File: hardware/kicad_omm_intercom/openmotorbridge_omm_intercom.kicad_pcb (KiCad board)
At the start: 2 copper layers, 60 x 30 mm, 18 parts, among them J1 TYPE-C-31-M-12_IP67, SW1 Power_MFB, SW2 Mesh_Group, SW3 Vol_Plus, SW4 Vol_Minus, U1 ESP32-C6-MINI-1U, U2 BQ24075RGTR, U3 XC6206P332MR, U4 ES8311_Codec

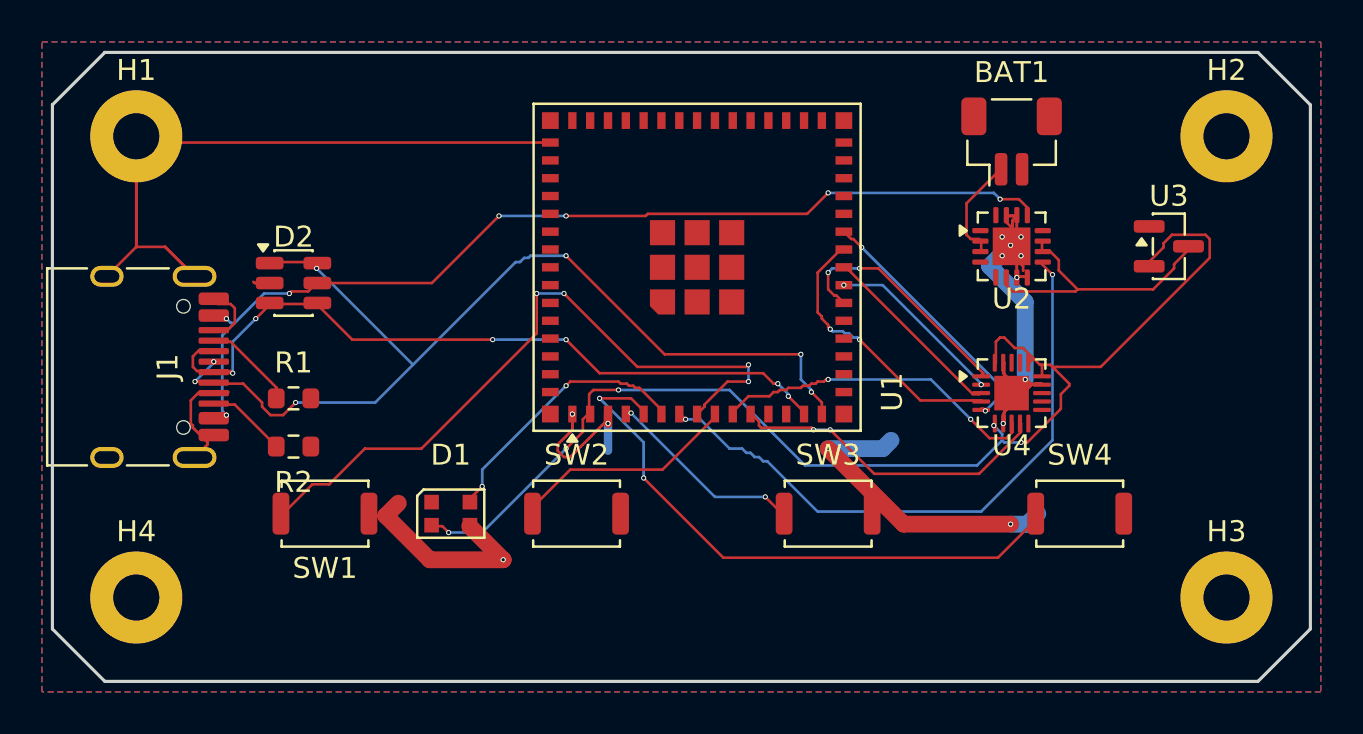
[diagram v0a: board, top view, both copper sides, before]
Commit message: feat(system): architecture refinement v6 across hardware, firmware and docs
- Hardware:
  * PCBA 09 (OMM 2.4 GHz Intercom): Upgrade to Everest Semi ES8388 stereo codec (QFN-28)
    and Multi-Use USB-C connector (J1) combining power, WebUSB flashing and stereo audio.
  * PCBA 08 (Radar 2.0 Sub-MCU): Strict HF hardening (2x U.FL: 6.5 GHz UWB & 5.9 GHz V2X;
    no 2.4 GHz/BLE at rear), right-angle 4-pin flashing header J3.
  * PCBA 03 (Cartridge): 8-pin Kelvin-grounded audio/power header with isolated PGND/AGND.
  * CAD: Standardize DIN 934 hex nut pockets across module enclosures.

- Firmware:
  * UWB Backbone: Add multi-channel substream audio downlink (sub-channels 0/1 music,
    sub-channel 2 voice) and audio uplink packet definitions.
  * Smart Cartridge: Implement zero-latency (<1 ms) voice routing to intercom mic pin,
    A2DP music stream buffering for mesh group sharing, and 100 Hz upstream audio capture.
  * Central Box: Central DSP mixer ducking (-18 dB), voice activity detection (VAD), and
    multi-channel UWB dispatching.
  * OMM Module: Implement ES8388 stereo codec driver and I2S master duplex stream.
  * Radar Sub-MCU: Confirm 2.4 GHz RF disable and autonomous emergency strobe trigger (<1 ms).

- Documentation & WebApp:
  * Align DE & EN chapters (01, 02, 03, 04b, 07, 08, 14, 15, 16) with v6 specifications.
  * Update WebApp PWA System Builder with ES8388 stereo codec and OMM 446 PMR/DMR module.
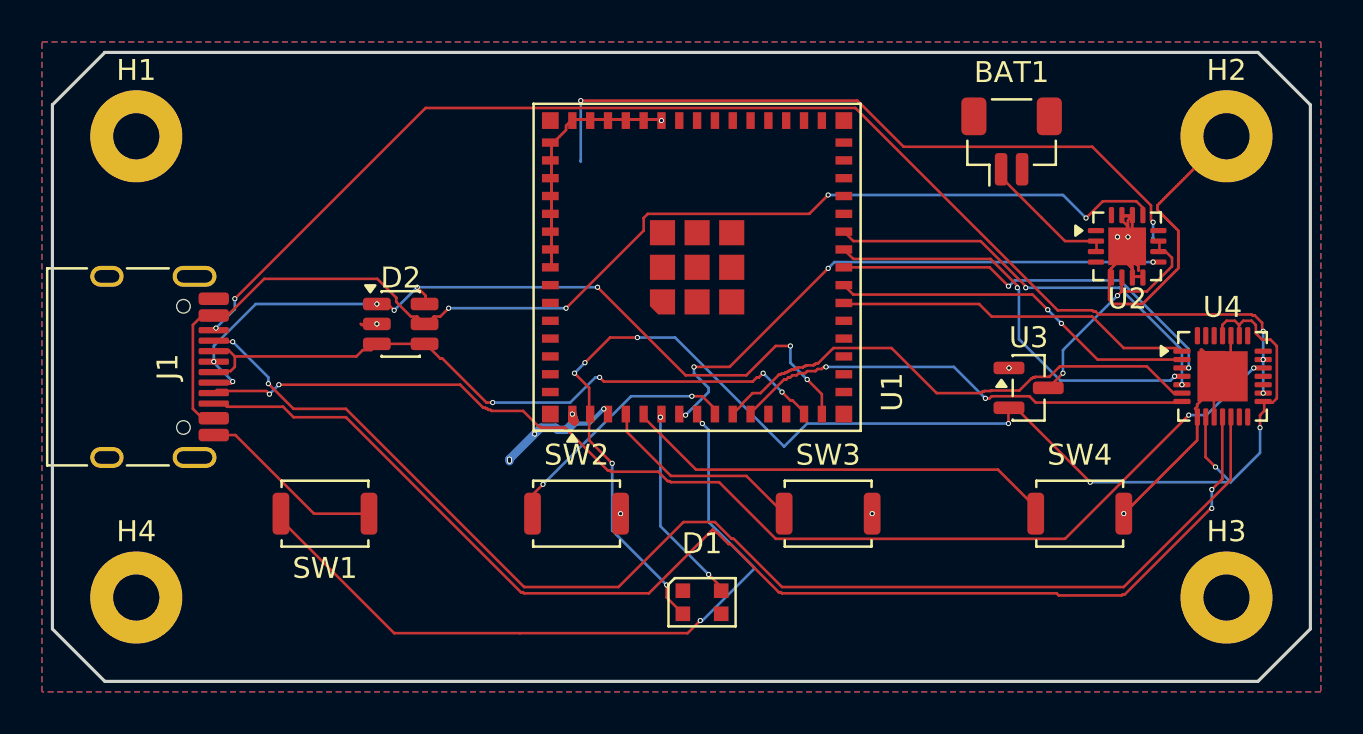
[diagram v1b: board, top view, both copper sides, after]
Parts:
- removed R1: 5.1k_CC1, R_0603_1608Metric
- removed R2: 5.1k_CC2, R_0603_1608Metric
- U4: value ES8311_Codec -> ES8388; footprint QFN-20-1EP_3x3mm_P0.4mm_EP1.65x1.65mm -> QFN-28-1EP_4x4mm_P0.4mm_EP2.4x2.4mm
- moved D1 12.7 mm to (101.0, 111.2)
- moved U4 10.1 mm to (125.8, 100.5)
- moved U3 9.50 mm to (116.6, 101.0)
- moved U2 5.51 mm to (121.3, 94.2)
- moved D2 5.47 mm to (86.6, 98.0)
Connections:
- net HP_OUT_N renamed MICBIAS
- net HP_OUT_P renamed VREF
- J1 pad : GND -> (no net)
- J1 pad A5: USB_CC1 -> HP_OUT_L
- J1 pad A8: GND -> MIC_IN+
- J1 pad B5: USB_CC2 -> HP_OUT_R
- J1 pad B8: GND -> AGND_SPK
- U4 pad : (no net) -> GND
- U4 pad 10: (no net) -> GND
- U4 pad 11: MIC_IN_P -> HP_OUT_R
- U4 pad 12: MIC_IN_N -> HP_OUT_L
- U4 pad 14: GND -> (no net)
- U4 pad 16: VCC_3V3 -> AGND_SPK
- U4 pad 19: GND -> MIC_IN+
- U4 pad 20: VCC_3V3 -> AGND_SPK
- U4 pad 21: GND -> (no net)
- U4 pad 6: VCC_3V3 -> I2C_SDA
- U4 pad 7: GND -> I2C_SCL
- U4 pad 8: I2C_SDA -> GND
- U4 pad 9: I2C_SCL -> VCC_3V3
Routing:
- net AGND_SPK: track 0.00 -> 62.3 mm, vias 0 -> 5
- net HP_OUT_L: track 0.00 -> 61.3 mm, vias 0 -> 2
- net HP_OUT_R: track 0.00 -> 59.5 mm, vias 0 -> 2
- net MIC_IN+: track 0.00 -> 56.8 mm, vias 0 -> 4
- net I2S_WS: track 9.19 -> 19.5 mm, vias 0 -> 2
- net I2S_BCLK: track 8.45 -> 17.6 mm
- net VBUS_5V: track 47.7 -> 56.8 mm, vias 7 -> 4
- net I2C_SDA: track 15.9 -> 24.7 mm, vias 2 -> 0
- net I2S_DIN: track 12.2 -> 20.2 mm
- net USB_DP: track 47.9 -> 40.1 mm, vias 7 -> 8
- net BTN_VOL_DOWN: track 28.5 -> 21.0 mm, vias 2 -> 0
- net I2C_SCL: track 15.5 -> 22.4 mm
- net I2S_DOUT: track 13.4 -> 20.2 mm
- net VCC_3V3: track 59.9 -> 66.7 mm, vias 5 -> 9
- net I2S_MCLK: track 11.7 -> 17.1 mm, vias 2 -> 0
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
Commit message: feat(hw): finalize PCBA 09 OMM 2.4 GHz routing parity, schematic, 3D renders, and JLCPCB package
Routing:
- net GND: track 112.9 -> 146.3 mm, vias 15 -> 14
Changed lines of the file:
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@@
 	)
 	(segment
-		(start 84.7 97.94)
-		(end 84.76 98)
-		(width 0.127)
-		(layer "F.Cu")
-		(net "GND")
-	)
-	(segment
 		(start 93.8 91.9)
 		(end 93.8 92)
@@
 	)
 	(via
-		(at 93 103.2)
-		(size 0.25)
-		(drill 0.15)
-		(layers "F.Cu" "B.Cu")
-		(net "GND")
-	)
-	(via
 		(at 96.3 102)
 		(size 0.25)
@@
 	)
 	(via
-		(at 97.1 107)
-		(size 0.25)
-		(drill 0.15)
-		(layers "F.Cu" "B.Cu")
-		(net "GND")
-	)
-	(via
-		(at 91.8 104.5)
-		(size 0.25)
-		(drill 0.15)
-		(layers "F.Cu" "B.Cu")
-		(net "GND")
-	)
-	(via
 		(at 115.625 100.05)
 		(size 0.25)
@@
 		(net "MIC_IN+")
 	)
+	(segment
+		(start 76.78 95.68)
+		(end 77.695 96.75)
+		(width 0.25)
+		(layer "F.Cu")
+		(net "GND")
+	)
+	(segment
+		(start 72.6 95.68)
+		(end 76.78 95.68)
+		(width 0.3)
+		(layer "F.Cu")
+		(net "GND")
+	)
+	(segment
+		(start 72.6 104.32)
+		(end 76.78 104.32)
+		(width 0.3)
+		(layer "F.Cu")
+		(net "GND")
+	)
+	(segment
+		(start 76.78 104.32)
+		(end 77.695 103.25)
+		(width 0.25)
+		(layer "F.Cu")
+		(net "GND")
+	)
+	(segment
+		(start 72.6 95.68)
+		(end 72.6 104.32)
+		(width 0.3)
+		(layer "B.Cu")
+		(net "GND")
+	)
+	(segment
+		(start 113.95 88.05)
+		(end 113.95 87.0)
+		(width 0.25)
+		(layer "F.Cu")
+		(net "GND")
+	)
+	(segment
+		(start 113.95 87.0)
+		(end 117.55 87.0)
+		(width 0.25)
+		(layer "F.Cu")
+		(net "GND")
+	)
+	(segment
+		(start 117.55 87.0)
+		(end 117.55 88.05)
+		(width 0.25)
+		(layer "F.Cu")
+		(net "GND")
+	)
+	(segment
+		(start 117.55 88.05)
+		(end 117.55 89.3)
+		(width 0.25)
+		(layer "F.Cu")
+		(net "GND")
+	)
+	(segment
+		(start 117.55 89.3)
+		(end 116.25 90.575)
+		(width 0.25)
+		(layer "F.Cu")
+		(net "GND")
+	)
+	(segment
+		(start 119.775 95)
+		(end 120.4 95.4)
+		(width 0.2)
+		(layer "F.Cu")
+		(net "GND")
+	)
+	(segment
+		(start 97.1 107.0)
+		(end 98.0 106.0)
+		(width 0.2)
+		(layer "F.Cu")
+		(net "GND")
+	)
+	(via
+		(at 98.0 106.0)
+		(size 0.25)
+		(drill 0.15)
+		(layers "F.Cu" "B.Cu")
+		(net "GND")
+	)
+	(segment
+		(start 101.9 111.775)
+		(end 101.9 112.5)
+		(width 0.2)
+		(layer "F.Cu")
+		(net "GND")
+	)
+	(via
+		(at 101.9 112.5)
+		(size 0.25)
+		(drill 0.15)
+		(layers "F.Cu" "B.Cu")
+		(net "GND")
+	)
+	(segment
+		(start 93.0 103.2)
+		(end 94.8 102.25)
+		(width 0.2)
+		(layer "B.Cu")
+		(net "GND")
+	)
 	(zone
 		(net "GND")
@@
 			(clearance 0.5)
 		)
-		(min_thickness 0.25)
+		(min_thickness 0.127)
 		(fill yes
 			(thermal_gap 0.18)
@@
 			(clearance 0.5)
 		)
-		(min_thickness 0.25)
+		(min_thickness 0.127)
 		(fill yes
 			(thermal_gap 0.18)

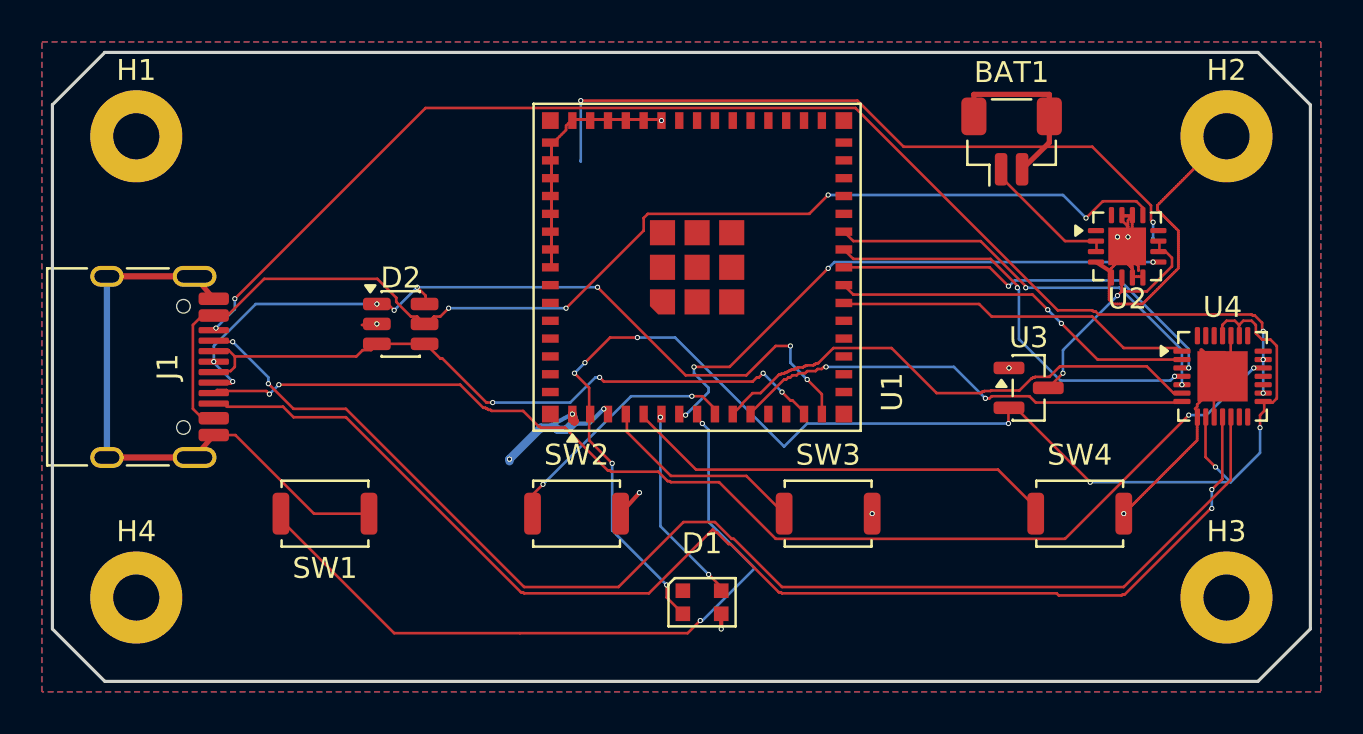
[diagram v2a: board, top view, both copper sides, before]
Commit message: feat(hw,docs): implement Dual-Engine OMB Lite architecture for PCBA 09 and PCBA 10
- Schematic: Add ESP32-PICO-V3-02 (BT Classic/BLE co-processor) and Johanson 2450AT18 chip antenna
- PCB: Add Grobplatzierung and Vorverbindung nets on B.Cu for PCBA 09 and PCBA 10
- Firmware: Add co-processor UART link config and disable BT on C6 to eliminate CoEx time-slicing
- Documentation: Add Dual-Engine architecture, Cardo DMC Bridge / Sena Bridge, and Profile C OMB Lite
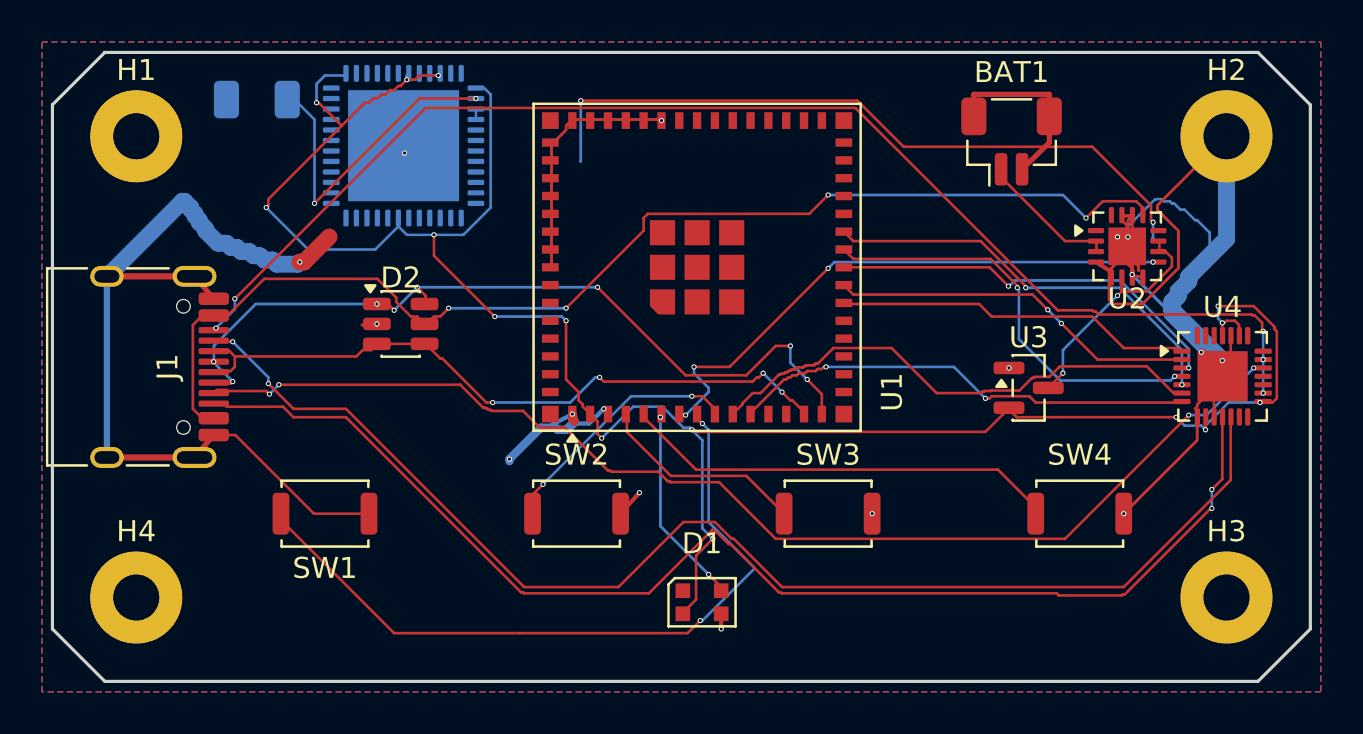
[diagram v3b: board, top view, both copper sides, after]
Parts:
- added ANT1: 2.45GHz_Chip_Antenna, RF_Antenna:Johanson_2450AT18x100, B.Cu at (79.8, 87.2)
- added U5: ESP32-PICO-V3-02, Package_DFN_QFN:QFN-48-1EP_7x7mm_P0.5mm_EP5.3x5.3mm, B.Cu at (86.8, 89.5)
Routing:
- net GND: track 146.3 -> 260.3 mm, vias 14 -> 19
- net VCC_3V3: track 66.7 -> 105.3 mm, vias 9 -> 15
- net BT_ANT: track 0.00 -> 15.5 mm, vias 0 -> 2

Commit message: feat(omm): set compact stubby antenna as helmet default, add internal J_HELMET audio & maintain external USB-C
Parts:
- added J_HELMET: HELMET_AUDIO_6P, JST_SH_SM06B-SRSS-TB_1x06-1MP_P1.00mm_Horizontal, B.Cu at (76.5, 104.0)
- added J_RF: U.FL-R-SMT-1, U.FL_Hirose_U.FL-R-SMT-1_Vertical, B.Cu at (126.0, 100.2)

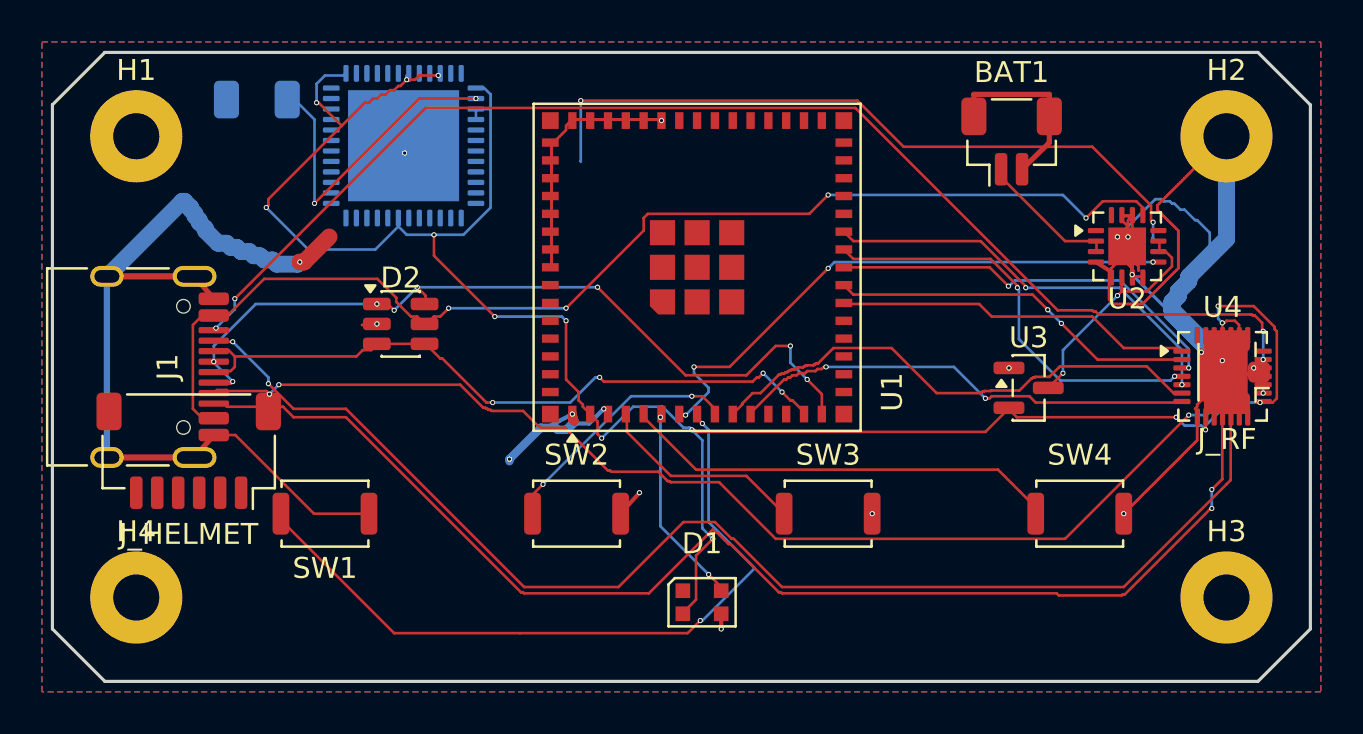
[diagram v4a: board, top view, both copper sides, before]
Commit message: fix(omm): align CAD, BOM and CPL with user re-routed PCBA 09 J_HELMET position opposite USB-C
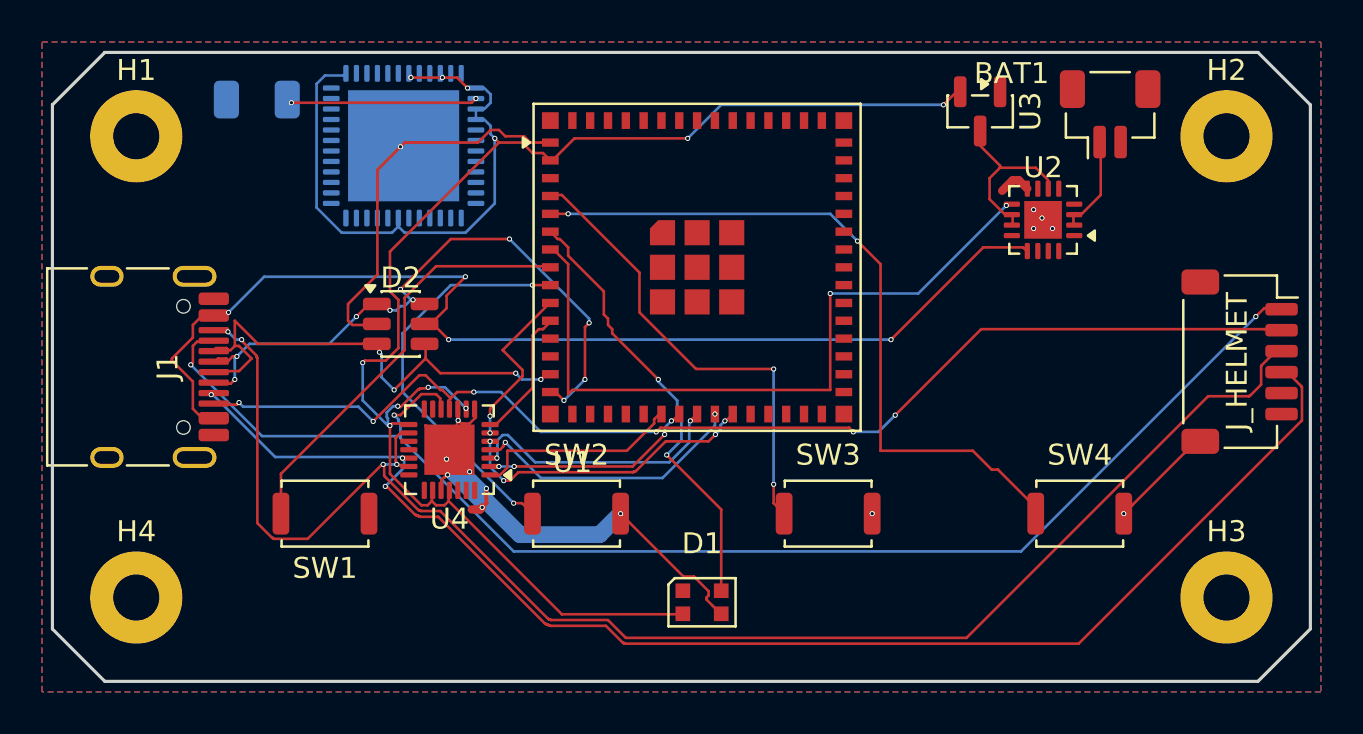
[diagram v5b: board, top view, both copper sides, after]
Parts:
- removed J_RF: U.FL-R-SMT-1, U.FL_Hirose_U.FL-R-SMT-1_Vertical
- moved J_HELMET 50.3 mm to (126.6, 99.8), turned to -90 degrees
- moved U4 37.0 mm to (88.9, 104.0), turned to 180 degrees
- moved U3 13.4 mm to (114.2, 87.8), turned to -90 degrees
- moved BAT1 4.88 mm to (120.5, 88.0)
- moved U2 4.21 mm to (117.2, 93.0), turned to 180 degrees
- turned U1 to 0 degrees
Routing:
- net GND: track 260.3 -> 57.3 mm, vias 19 -> 14
- net I2C_SDA: track 24.7 -> 8.17 mm, vias 0 -> 2
- net I2C_SCL: track 22.4 -> 6.09 mm, vias 2 -> 0
- net BTN_PWR: track 35.0 -> 20.4 mm, vias 2 -> 0
- net BTN_VOL_DOWN: track 21.0 -> 34.1 mm, vias 0 -> 2
- net BTN_VOL_UP: track 10.1 -> 22.3 mm, vias 0 -> 2
- net AGND_SPK: track 62.3 -> 73.7 mm, vias 5 -> 4
- net WS2812_DATA: track 9.80 -> 20.9 mm
- net USB_DP: track 40.1 -> 29.4 mm, vias 8 -> 10
- net VCC_3V3: track 105.3 -> 94.7 mm, vias 15 -> 11
- net USB_DN: track 33.1 -> 23.5 mm
- net MIC_IN+: track 56.8 -> 65.9 mm, vias 4 -> 3
- net I2S_MCLK: track 17.1 -> 9.53 mm
- net BTN_MESH: track 12.0 -> 19.5 mm
- net I2S_BCLK: track 17.6 -> 10.2 mm, vias 2 -> 4
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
